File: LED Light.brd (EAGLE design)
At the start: 101.6 x 55.9 mm, 13 parts, among them J1 AVR_SPI_PRG_6NS, U1 Tiny85-20-SMT

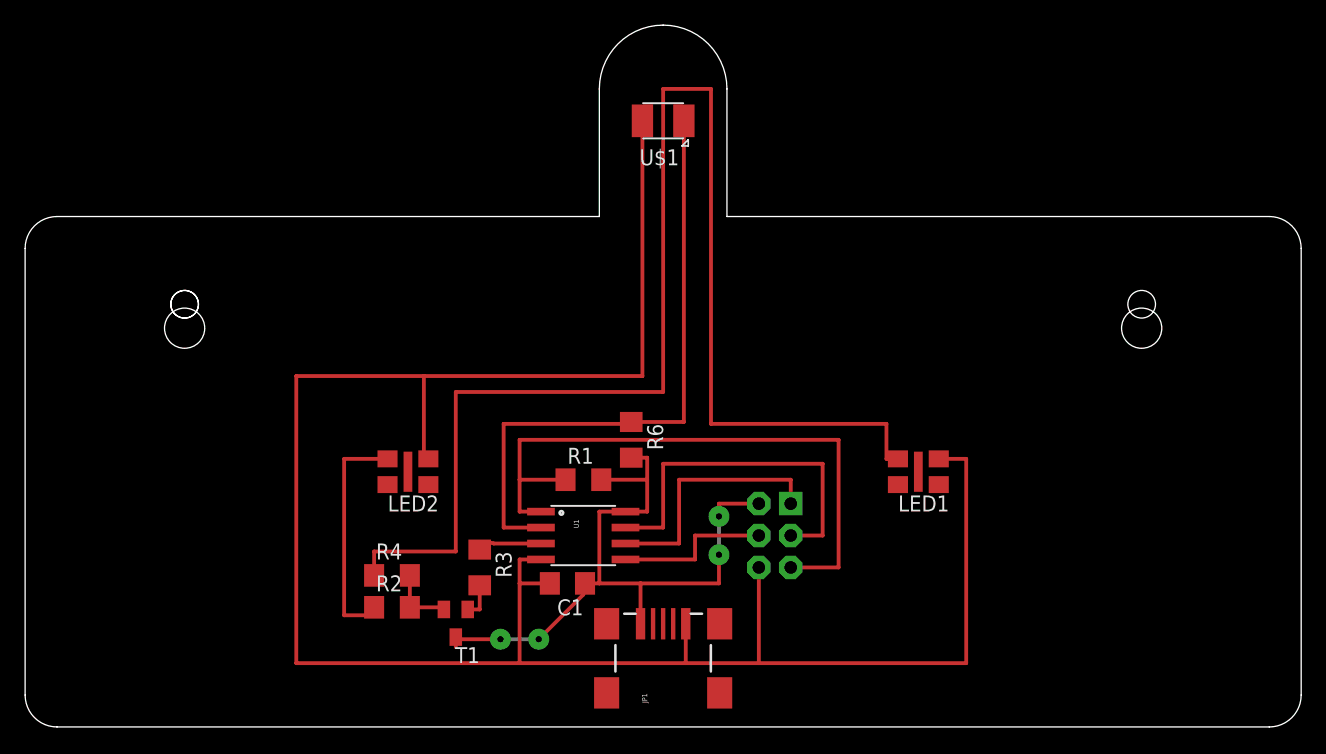
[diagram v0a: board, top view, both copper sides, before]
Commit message: Initial work on board layout. Still missing mic circuit.
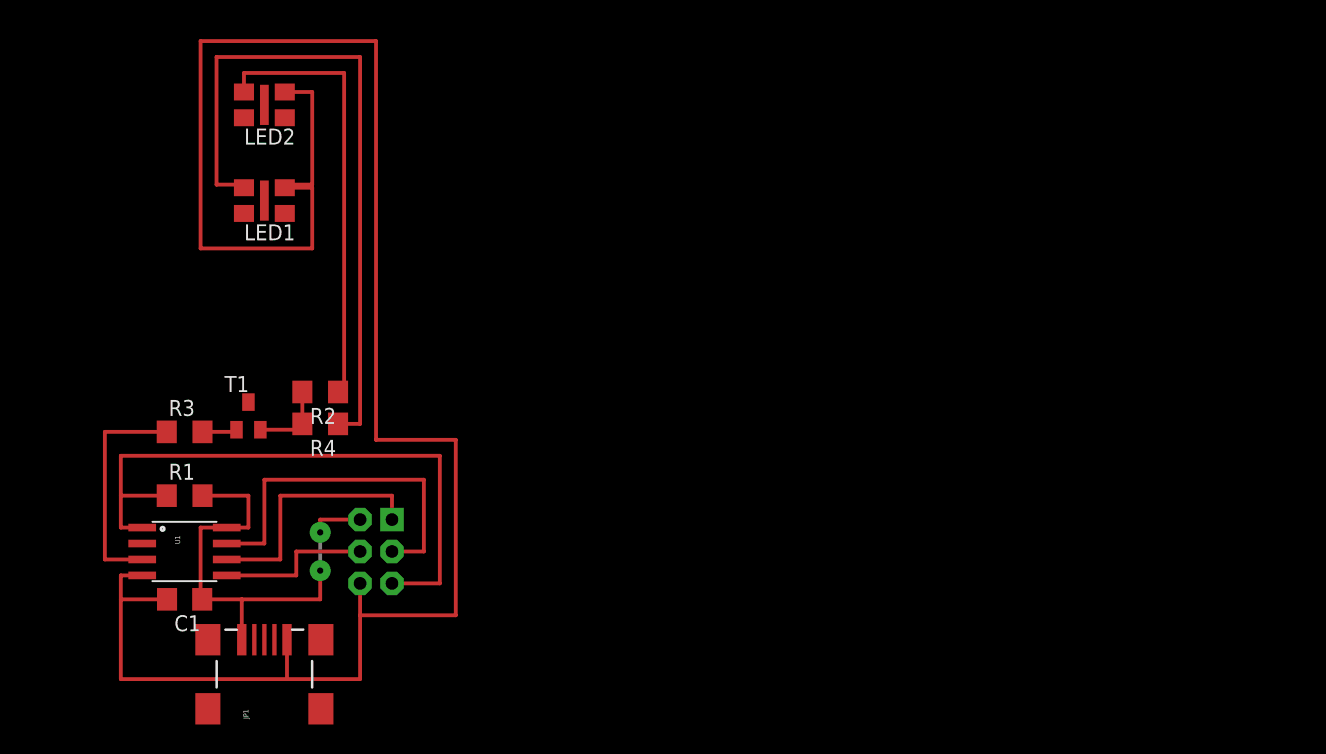
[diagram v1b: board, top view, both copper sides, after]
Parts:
- removed R6: 49.9K, rcl:R1206
- removed U$1: PHOTOTRANSISTOR-NPN-OP580AD, LED Light:OP580DA
- moved LED1 56.4 mm to (19.1, 41.9)
- moved R1 31.8 mm to (12.7, 18.4)
- moved U1 31.8 mm to (12.7, 14.0)
- moved J1 31.8 mm to (27.9, 14.0)
- moved JP1 31.8 mm to (19.1, 3.17)
- moved LED2 31.4 mm to (19.1, 49.5)
- moved C1 30.5 mm to (12.7, 10.2)
- moved R3 25.9 mm to (12.7, 23.5), turned to 0 degrees
- moved T1 23.3 mm to (17.8, 24.8), turned to 0 degrees
- moved R2 18.1 mm to (23.5, 26.7), turned to 180 degrees
- moved R4 13.4 mm to (23.5, 24.1), turned to 180 degrees
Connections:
- net GND: no longer U$1.EMITTER
- net N$7: no longer R6.1, U$1.COLLECTOR
- net VCC: no longer R6.2
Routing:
- net N$5: track 109.9 -> 55.0 mm
- net N$7: track 49.7 -> 0.00 mm
- net VCC: track 55.7 -> 38.0 mm, vias 4 -> 2
- net N$3: track 18.9 -> 35.4 mm
- net N$4: track 4.98 -> 18.1 mm
- net GND: track 172.6 -> 161.5 mm
- net N$1: track 5.42 -> 6.35 mm
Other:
- board outline removed

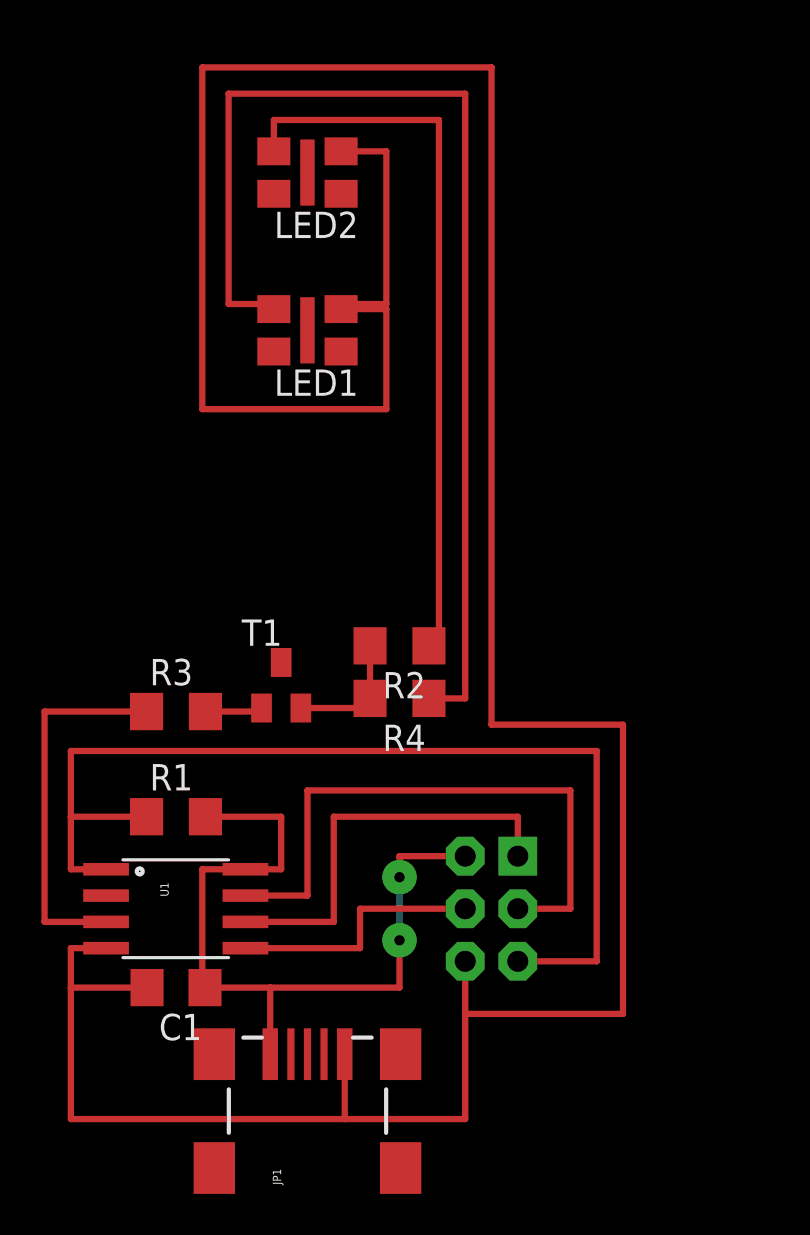
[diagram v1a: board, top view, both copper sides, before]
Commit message: Move LEDs to PWM pin (MOSI) and clean up layout.
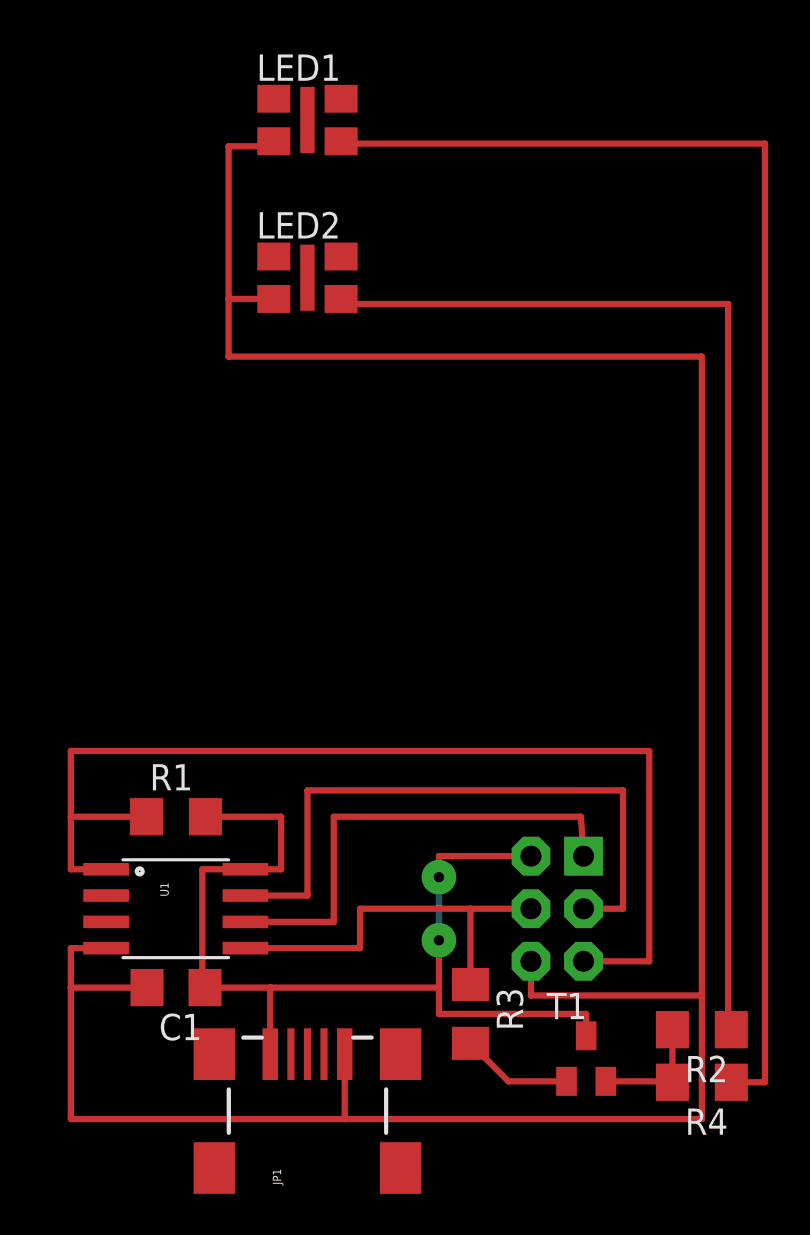
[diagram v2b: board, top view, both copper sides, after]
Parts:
- moved R2 23.6 mm to (38.1, 8.13)
- moved R4 23.6 mm to (38.1, 5.59)
- moved T1 23.3 mm to (32.5, 6.73)
- moved R3 20.4 mm to (26.9, 8.89), turned to 270 degrees
- moved LED1 10.2 mm to (19.1, 52.1), turned to 0 degrees
- moved LED2 5.08 mm to (19.1, 44.5), turned to 0 degrees
- moved J1 3.17 mm to (31.1, 14.0)
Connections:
- removed net N$4: R3.1, U1.3
- net MOSI: now also R3.1
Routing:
- net GND: track 161.5 -> 131.6 mm
- net N$3: track 35.4 -> 54.1 mm
- net N$4: track 18.1 -> 0.00 mm
- net VCC: track 38.0 -> 50.6 mm
- net N$5: track 55.0 -> 67.6 mm
- net MOSI: track 12.5 -> 19.4 mm
- net MISO: track 20.1 -> 23.2 mm
- net N$2: track 2.88 -> 5.40 mm
- net RESET: track 50.4 -> 52.3 mm
- net SCK: track 29.0 -> 30.9 mm
- net N$1: track 6.35 -> 5.80 mm

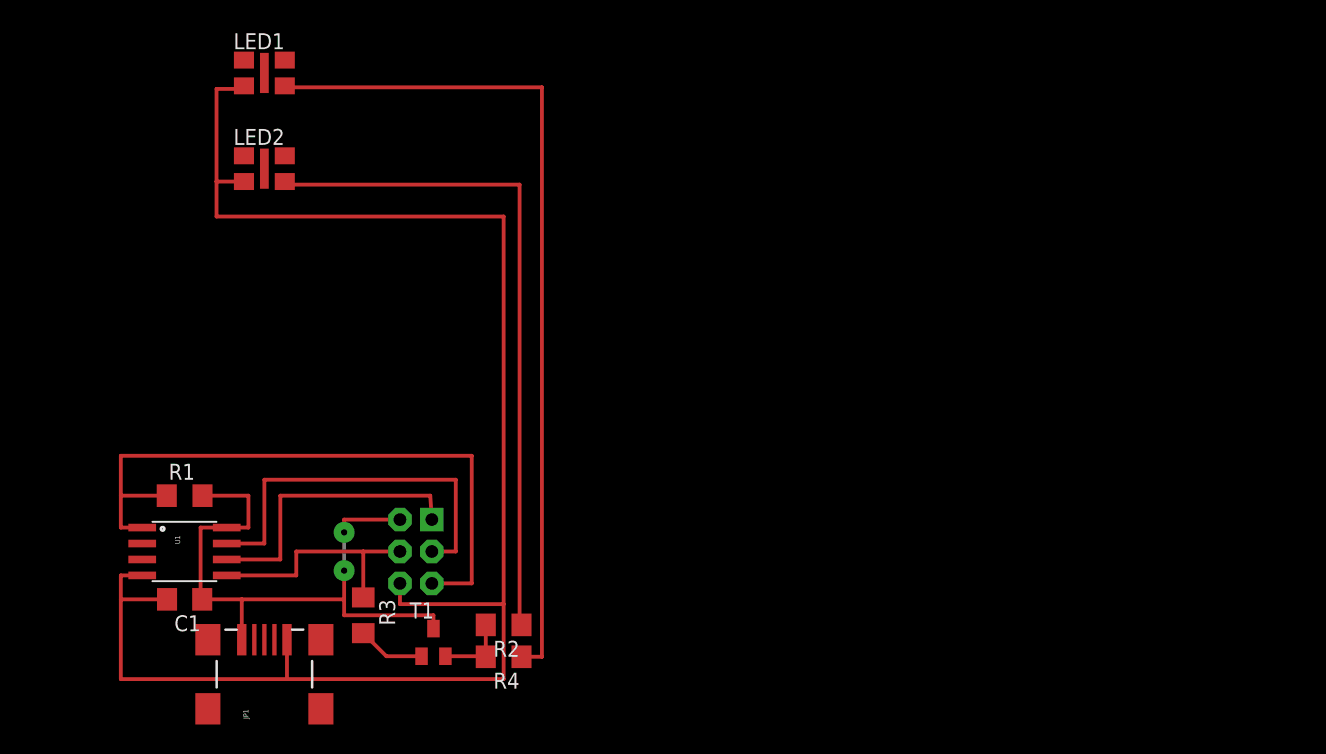
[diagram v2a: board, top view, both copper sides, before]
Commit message: Integrate mic into main board, layout in circle.
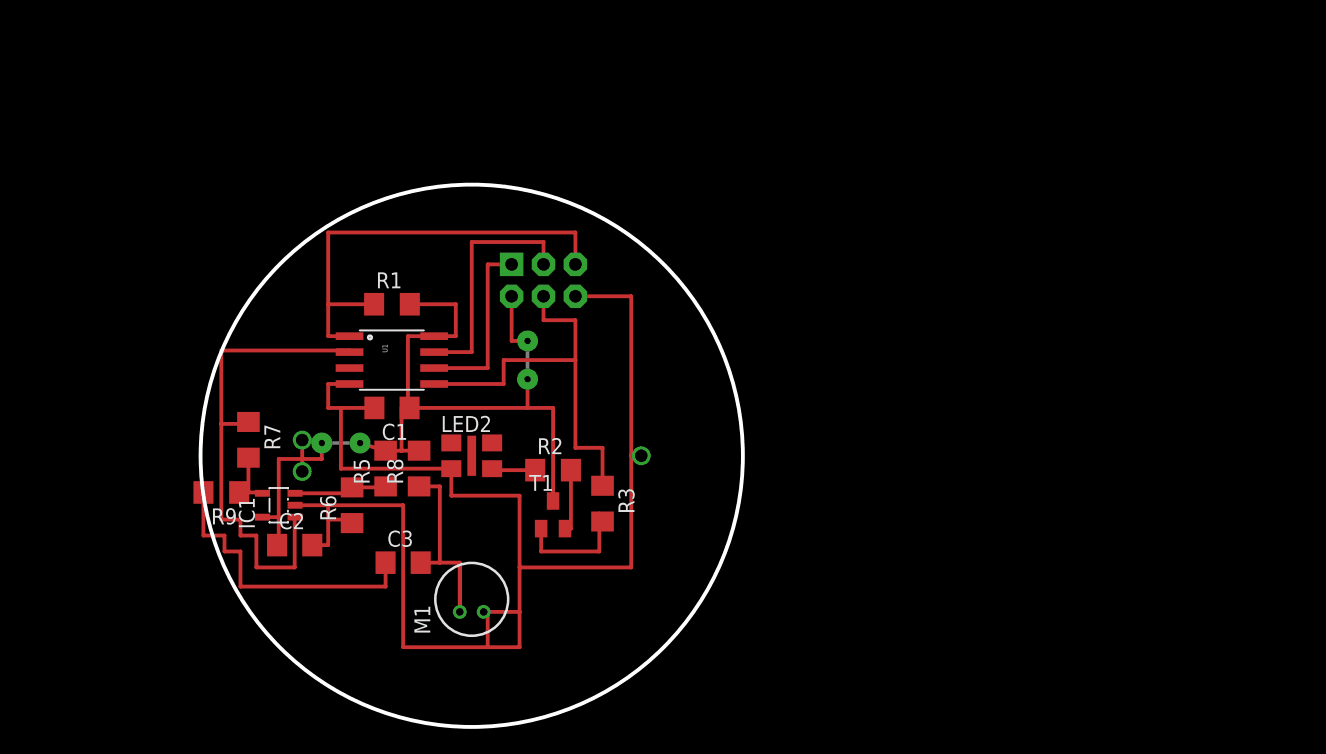
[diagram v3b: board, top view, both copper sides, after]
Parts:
- removed JP1: USB_MINIB-POWER, LED Light:USB_MINIB_POWER
- removed LED1: ML-EFAB, LED Light:ML-E-FAB
- removed R4: (no value), rcl:R1206
- added C2: 0.1uF, rcl:C1206
- added C3: 1uF, rcl:C1206
- added IC1: AD8614RJ, analog-devices:SOT23-5
- added M1: ELECTRET_MICROPHON-WM.64PN, microphon:WM-64PN
- added R5, R6, R7, R8: 10K, rcl:R1206
- added R9: 1K, rcl:R1206
- added U$1: BATTERY-CR2032, LED Light:CR2032_TH
- moved LED2 28.2 mm to (35.6, 21.6)
- moved J1 23.9 mm to (41.3, 35.6), turned to 180 degrees
- moved R1 22.5 mm to (29.2, 33.7)
- moved U1 22.5 mm to (29.2, 29.2)
- moved C1 22.5 mm to (29.2, 25.4)
- moved R3 21.0 mm to (46.0, 17.8)
- moved T1 13.9 mm to (42.0, 16.9)
- moved R2 12.9 mm to (42.0, 20.4), turned to 0 degrees
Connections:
- removed net N$5: LED1.A@1, R4.1
- removed net N$7: U1.2
- new net IN+: IC1.3, R5.1, R6.2
- new net IN-: IC1.4, R7.2, R9.1
- new net MIC: IC1.1, R7.1, U1.2
- new net N$4: C3.2, M1.1, R8.1
- new net N$6: C3.1, R9.2
- net GND: now also C2.2, IC1.2, M1.2, R6.1, U$1.-; no longer JP1.GND, LED1.C@1
- net N$1: no longer R4.2
- net VCC: now also C2.1, IC1.5, R5.2, R8.2, U$1.+, U$1.+'; no longer JP1.VBUS
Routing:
- net N$5: track 67.6 -> 0.00 mm
- net N$3: track 54.1 -> 3.55 mm
- net MIC: track 0.00 -> 39.8 mm
- net N$6: track 0.00 -> 23.9 mm
- net VCC: track 50.6 -> 73.9 mm, vias 2 -> 4
- net N$4: track 0.00 -> 18.3 mm
- net RESET: track 52.3 -> 35.8 mm
- net GND: track 131.6 -> 117.8 mm
- net MOSI: track 19.4 -> 32.9 mm
- net SCK: track 30.9 -> 19.3 mm
- net MISO: track 23.2 -> 14.4 mm
- net IN+: track 0.00 -> 7.76 mm
- net IN-: track 0.00 -> 5.42 mm
- net N$2: track 5.40 -> 10.2 mm
- net N$1: track 5.80 -> 5.13 mm
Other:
- board outline added: 43.2 x 43.2 mm
